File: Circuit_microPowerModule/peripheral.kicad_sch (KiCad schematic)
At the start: 26 parts, among them J4 Conn_01x05_Pin, J6 MikroBus

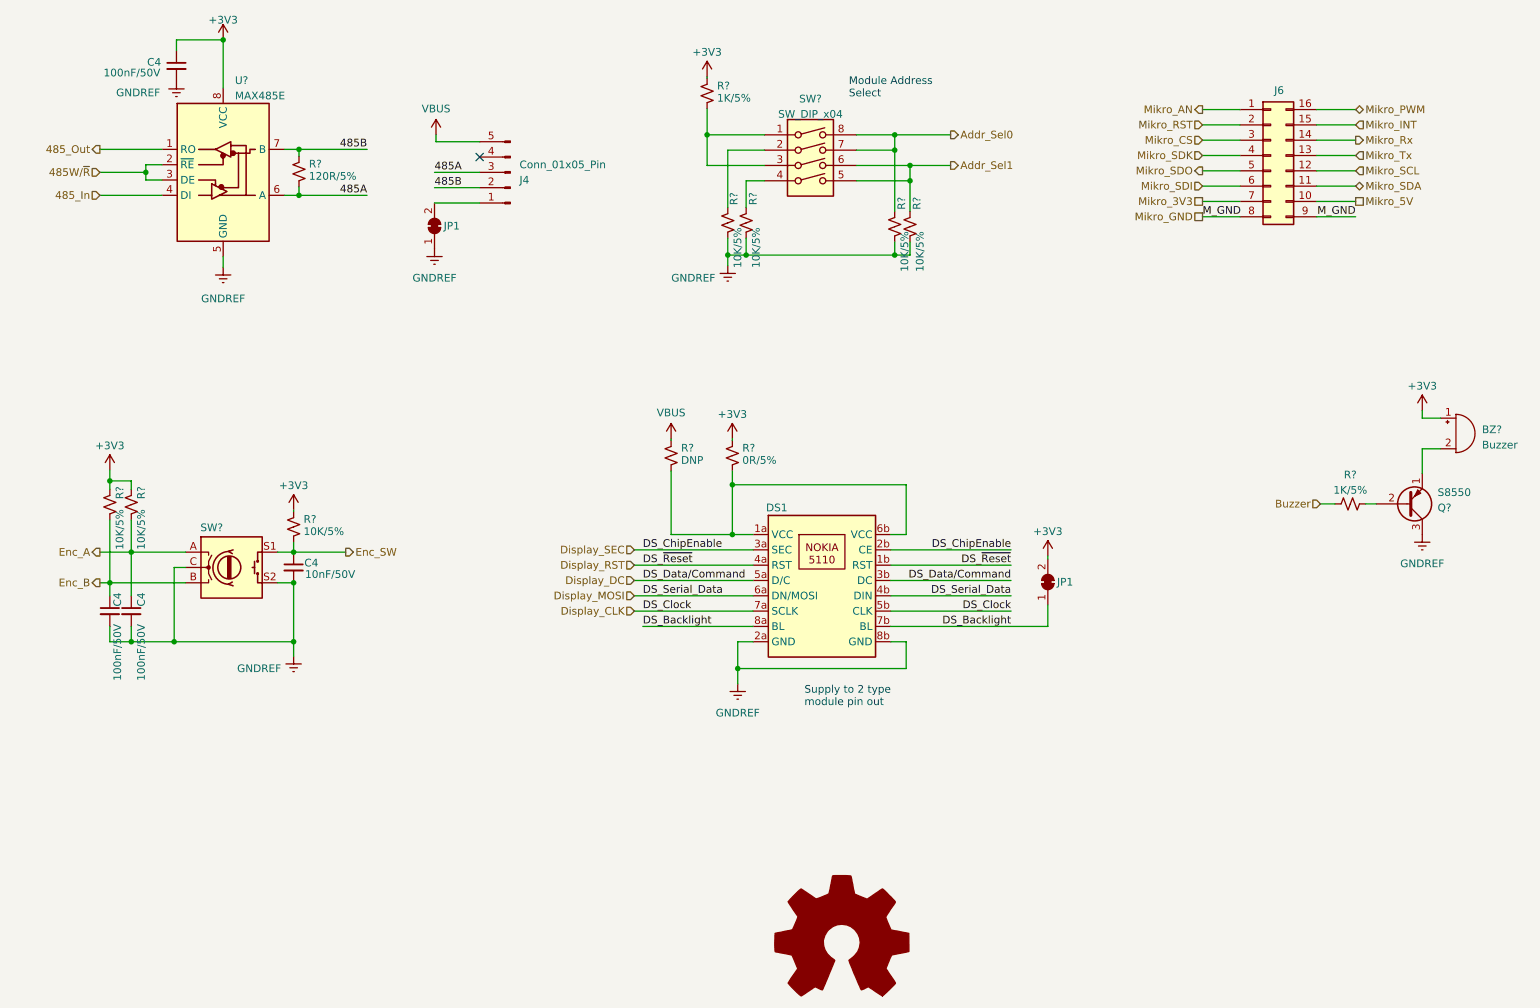
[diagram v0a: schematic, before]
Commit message: update schematic
added pin assessment to readme
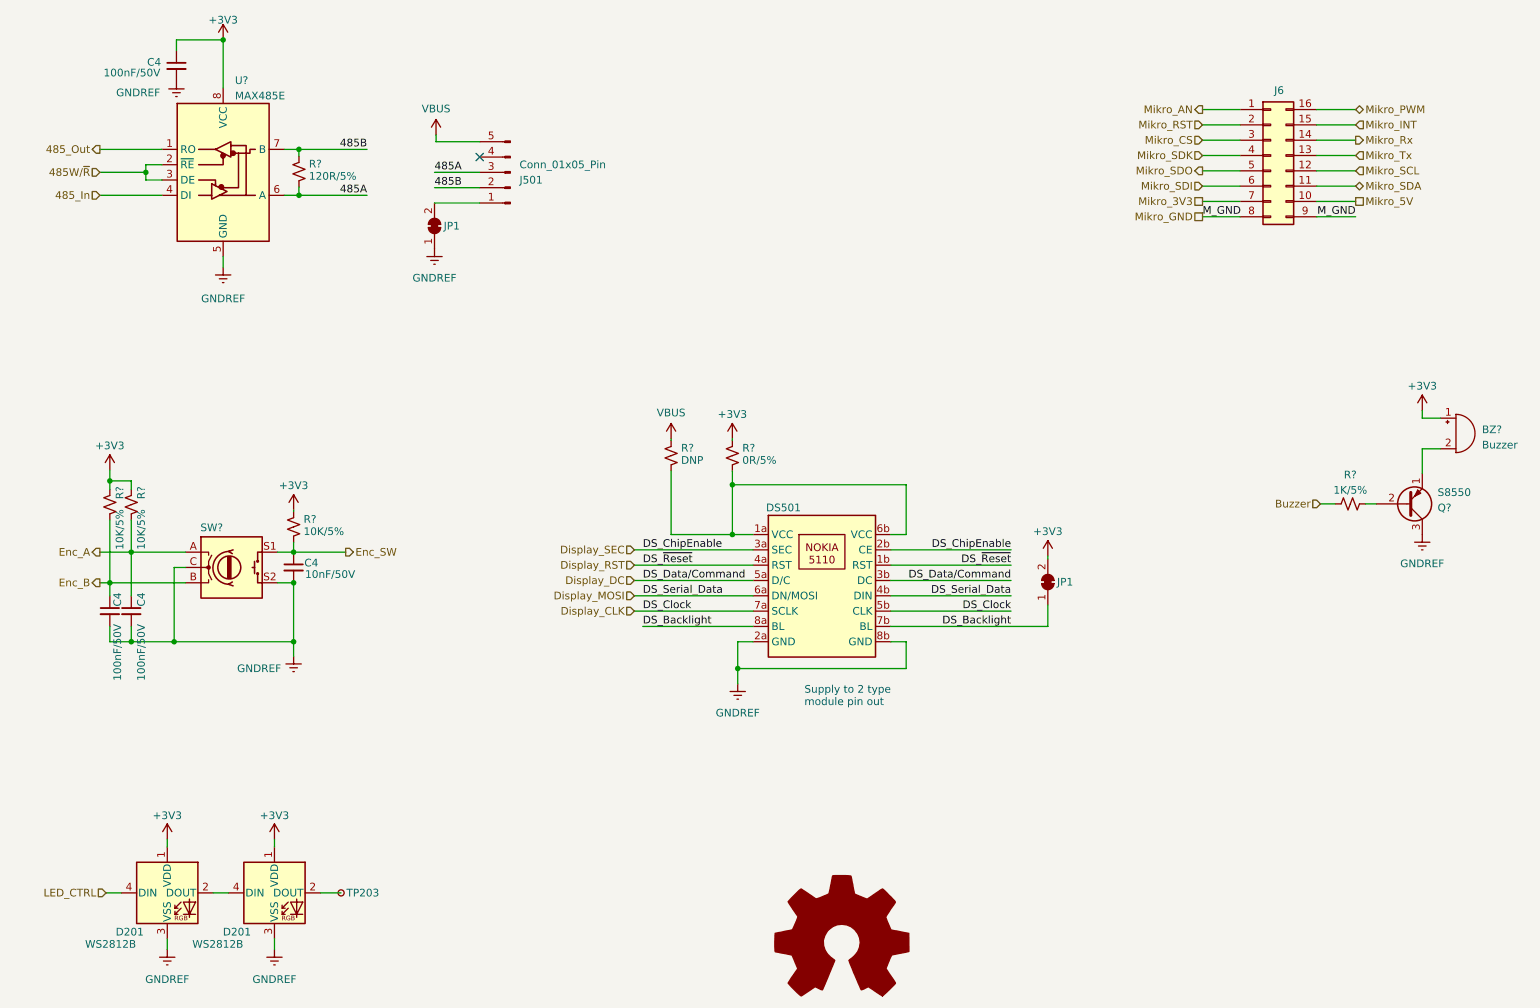
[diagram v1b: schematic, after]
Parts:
- removed R? (x4): 10K/5%, Resistor_SMD:R_0603_1608Metric, symbol Device:R_Small_US
- removed R?: 1K/5%, Resistor_SMD:R_0603_1608Metric, symbol Device:R_Small_US
- removed SW?: SW_DIP_x04, Button_Switch_SMD:SW_DIP_SPSTx04_Slide_Copal_CHS-04B_W7.62mm_P1.27mm, symbol Switch:SW_DIP_x04
- added D201 (x2): WS2812B, LED_SMD:LED_WS2812B_PLCC4_5.0x5.0mm_P3.2mm, symbol LED:WS2812B
- added TP203: TestPoint_Small, TestPoint:TestPoint_Keystone_5015_Micro-Minature, symbol Connector:TestPoint_Small
- renumbered DS1 to DS501, J4 to J501
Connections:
- net +3V3: now also D201.1 (VDD), D201.1 (VDD)
- net GNDREF: now also D201.3 (VSS), D201.3 (VSS)
- new net: D201.2 (DOUT), TP203.1
- new net: D201.2 (DOUT), D201.4 (DIN)
- new net LED_CTRL: D201.4 (DIN)

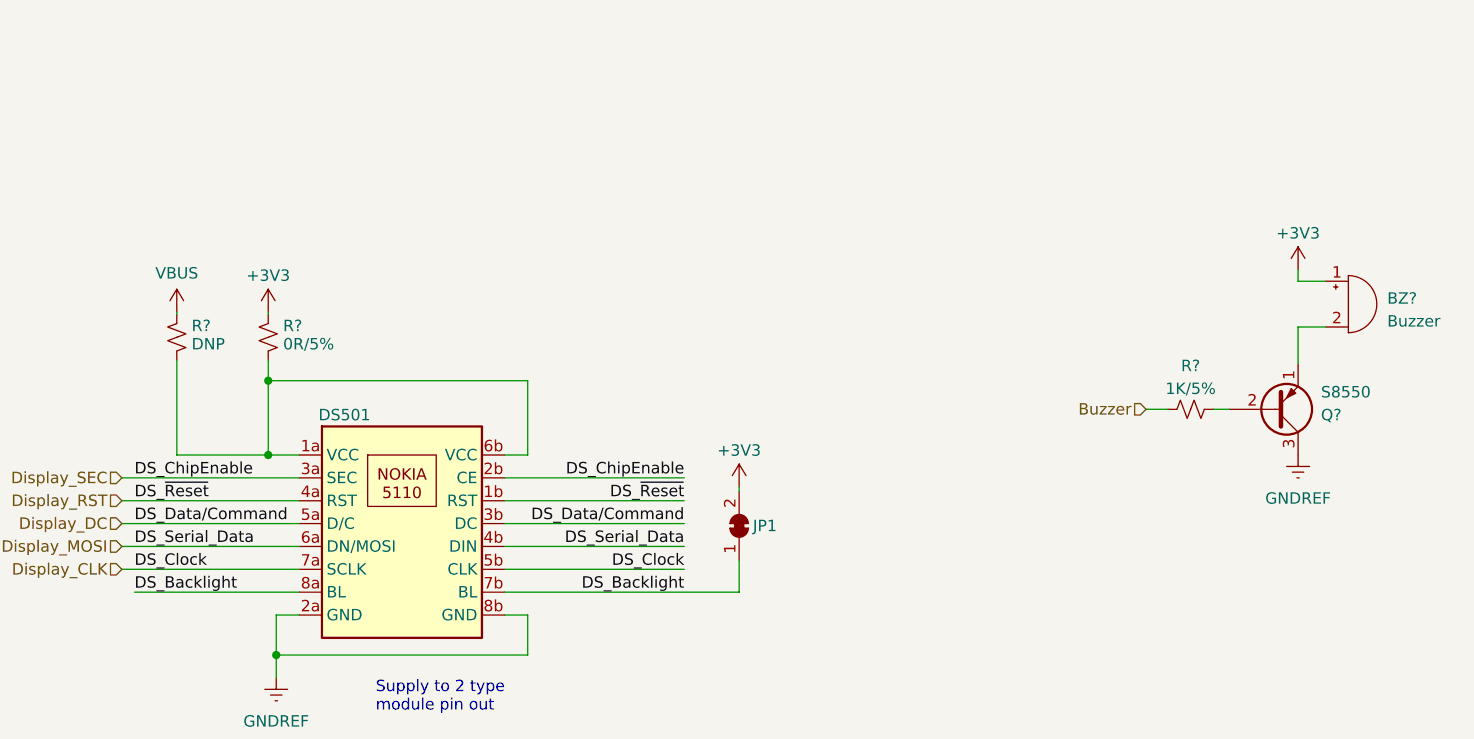
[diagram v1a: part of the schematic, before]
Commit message: modify ERC error, protect components
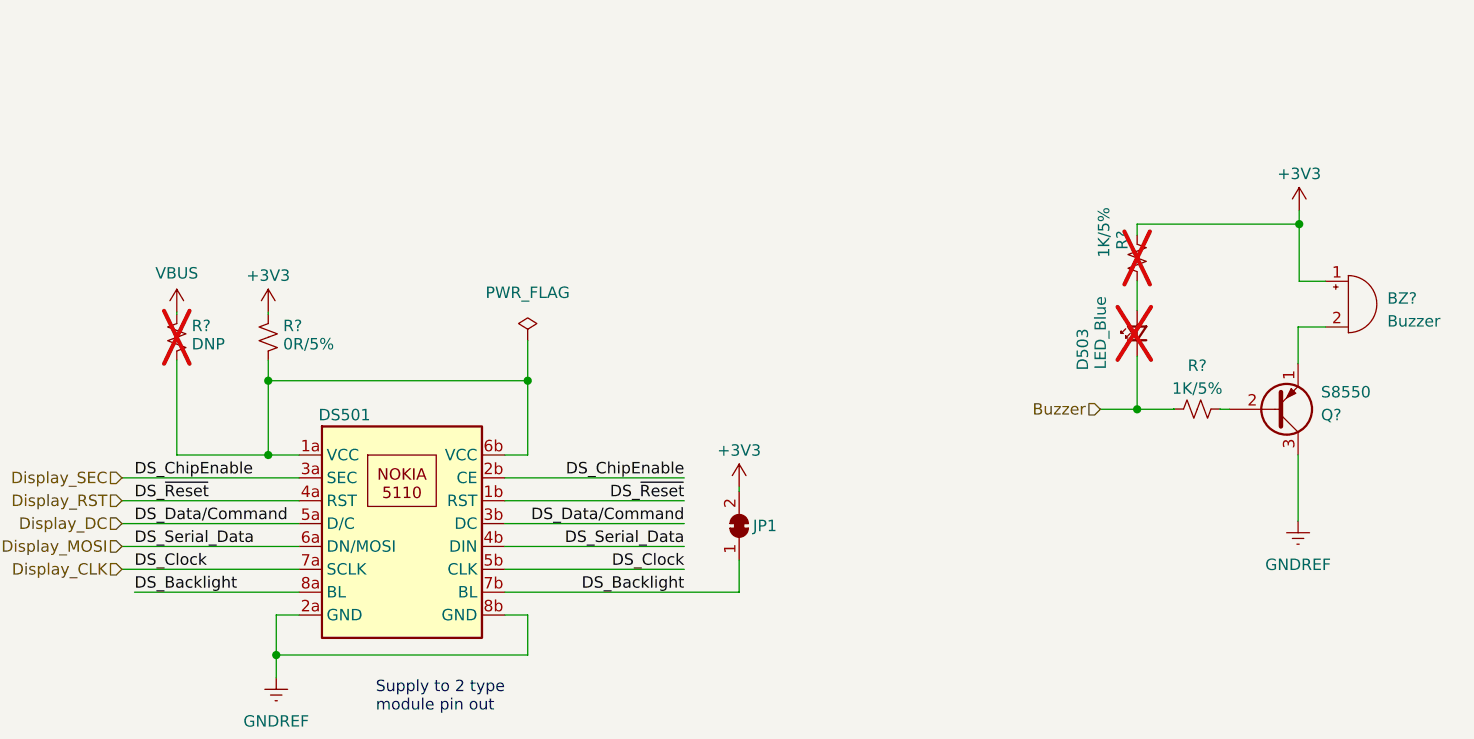
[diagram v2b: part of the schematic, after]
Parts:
- added D503: LED_Blue, LED_SMD:LED_1206_3216Metric, symbol Device:LED_Small
- added R?: 1K/5%, Resistor_SMD:R_0603_1608Metric, symbol Device:R_Small_US
- R?: now not fitted
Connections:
- net +3V3: now also R?.1
- net Buzzer: now also D503.1 (K)
- new net: D503.2 (A), R?.2
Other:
- title: (none) -> µPower Module
- moved on the sheet: R?

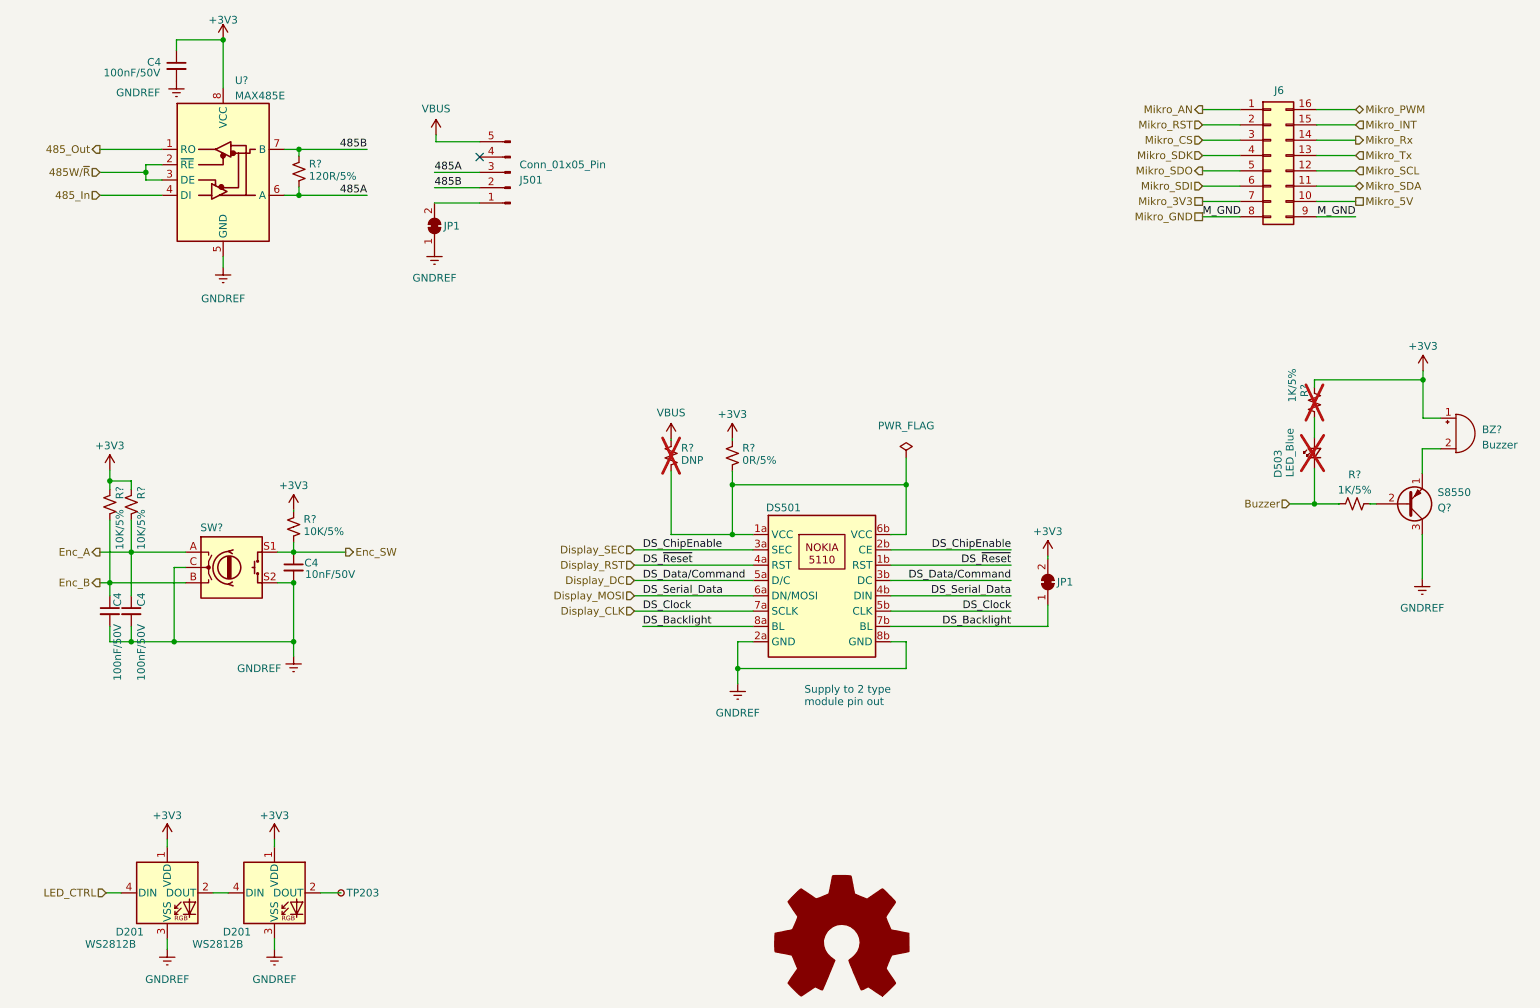
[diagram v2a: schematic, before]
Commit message: modify ERC warning
modify OPA, TVS-Diode, Cap
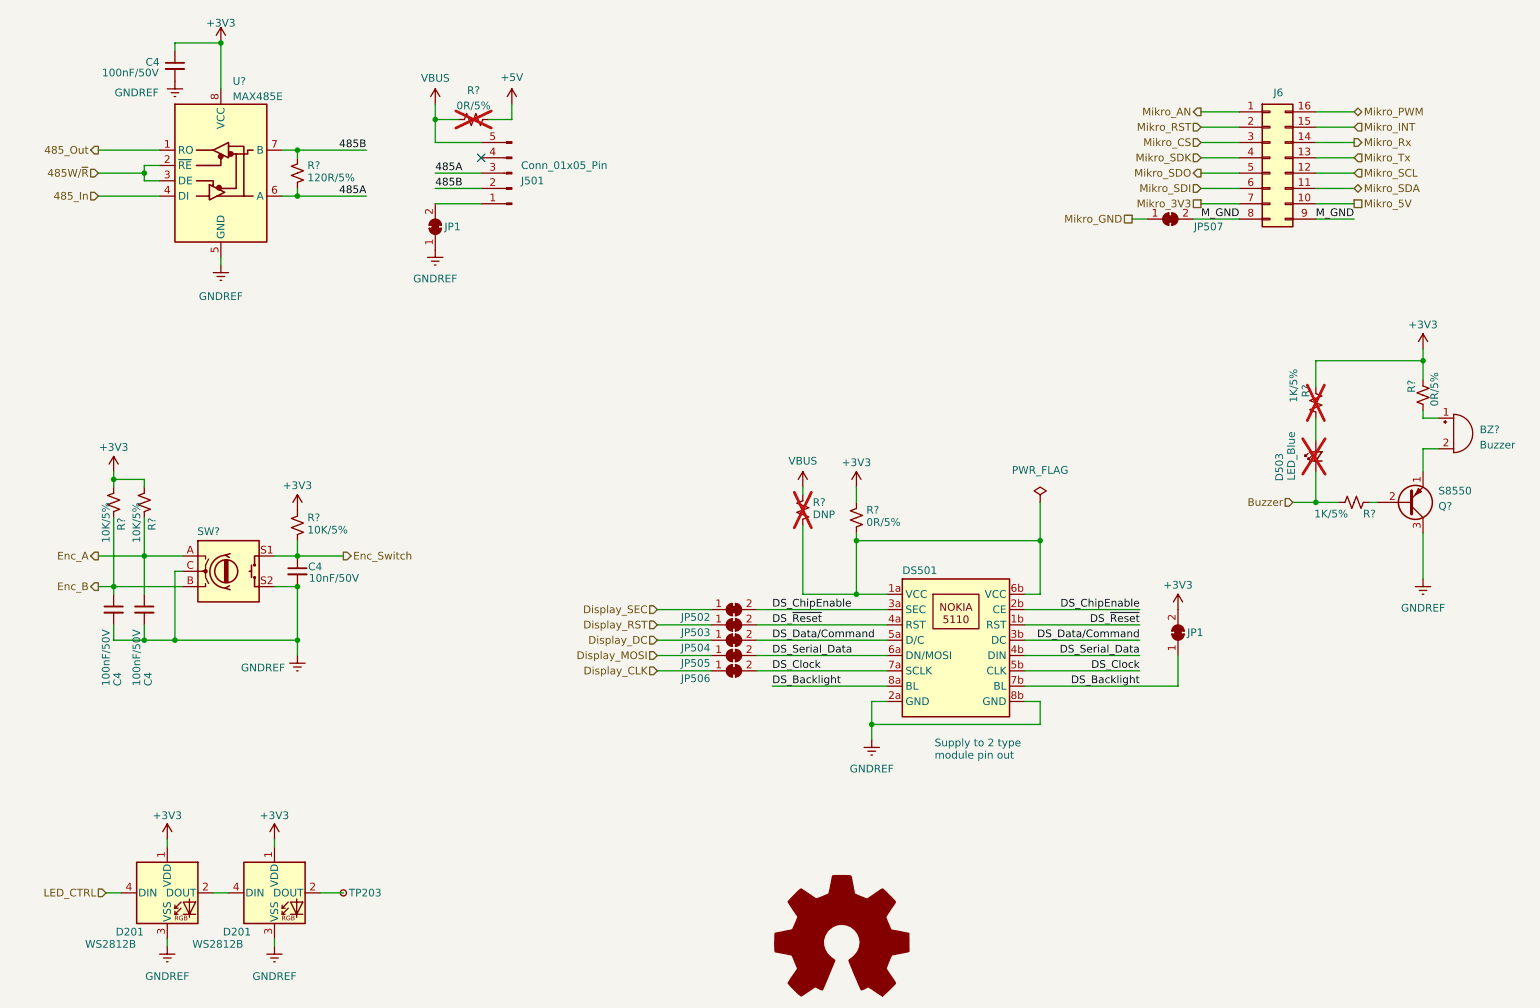
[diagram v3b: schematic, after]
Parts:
- added JP502, JP503, JP504, JP505, JP506, JP507: SolderJumper_2_Bridged, Jumper:SolderJumper-2_P1.3mm_Bridged_Pad1.0x1.5mm, symbol Jumper:SolderJumper_2_Bridged
- added R? (x2): 0R/5%, Resistor_SMD:R_0603_1608Metric, symbol Device:R_Small_US
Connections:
- net +3V3: now also R?.1; no longer BZ?.1 (-)
- net Display_CLK: now also JP506.1 (A); no longer DS501.5b (CLK), DS501.7a (SCLK)
- net Display_DC: now also JP504.1 (A); no longer DS501.3b (DC), DS501.5a (D/C)
- net Display_MOSI: now also JP505.1 (A); no longer DS501.4b (DIN), DS501.6a (DN/MOSI)
- net Display_RST: now also JP503.1 (A); no longer DS501.1b (RST), DS501.4a (RST)
- net Display_SEC: now also JP502.1 (A); no longer DS501.2b (CE), DS501.3a (SEC)
- net Mikro_GND: now also JP507.1 (A); no longer J6.8 (Pin_8), J6.9 (Pin_9)
- net VBUS: now also R?.1
- net Enc_SW renamed Enc_Switch
- new net: BZ?.1 (-), R?.2
- new net +5V: R?.2
- new net DS_ChipEnable: DS501.2b (CE), DS501.3a (SEC), JP502.2 (B)
- new net DS_Clock: DS501.5b (CLK), DS501.7a (SCLK), JP506.2 (B)
- new net DS_Data/Command: DS501.3b (DC), DS501.5a (D/C), JP504.2 (B)
- new net DS_Serial_Data: DS501.4b (DIN), DS501.6a (DN/MOSI), JP505.2 (B)
- new net DS_~{Reset}: DS501.1b (RST), DS501.4a (RST), JP503.2 (B)
- new net M_GND: J6.8 (Pin_8), J6.9 (Pin_9), JP507.2 (B)
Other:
- moved on the sheet: C4, D503, DS501, JP1, R?, SW?

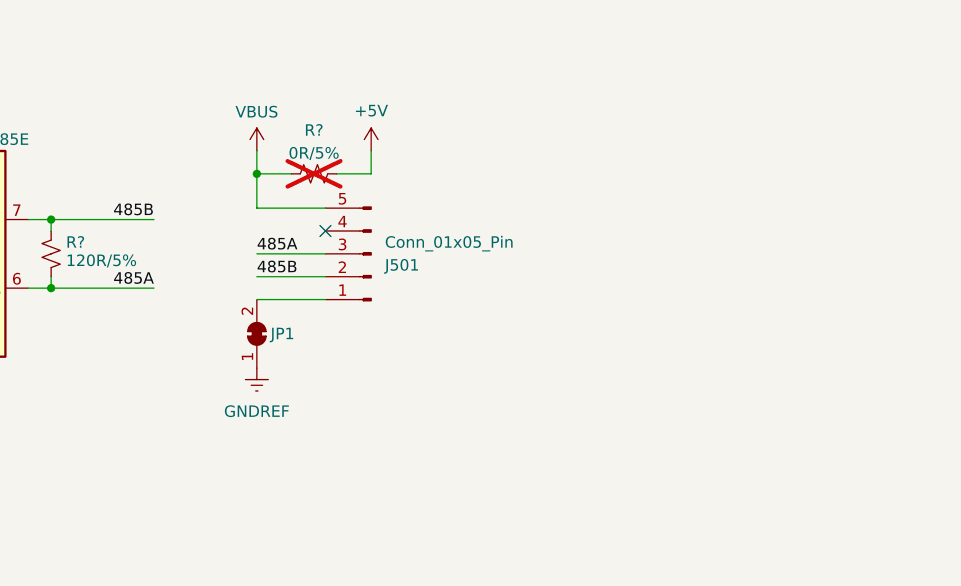
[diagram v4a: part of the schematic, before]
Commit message: update pcb layout component
target to smaller pcb size
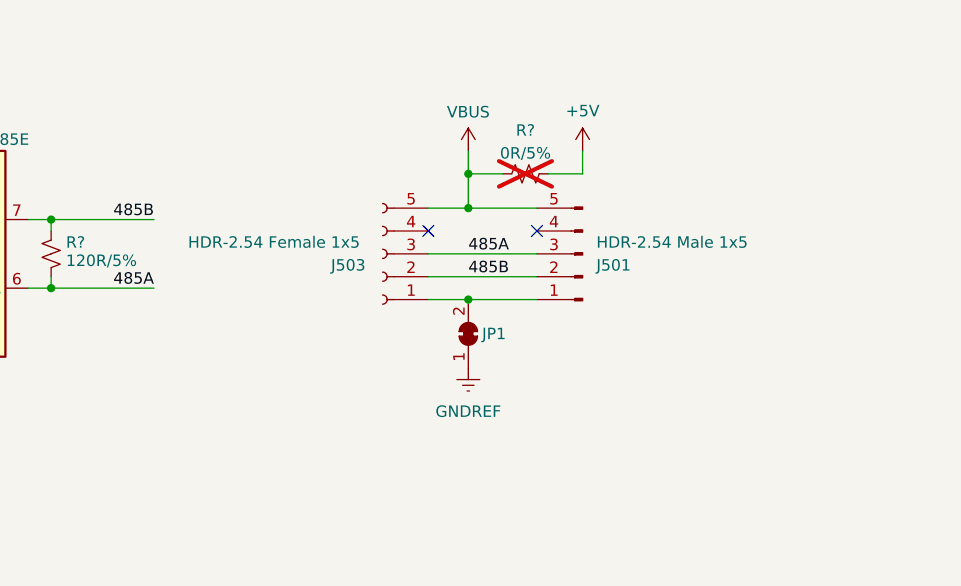
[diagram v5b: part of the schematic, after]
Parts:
- added J503: HDR-2.54 Female 1x5, Connector_PinSocket_2.54mm:PinSocket_1x05_P2.54mm_Vertical, symbol Connector:Conn_01x05_Socket
- J501: value Conn_01x05_Pin -> HDR-2.54 Male 1x5
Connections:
- net 485A: now also J503.3 (Pin_3)
- net 485B: now also J503.2 (Pin_2)
- net VBUS: now also J503.5 (Pin_5)
- net at J501.1 (Pin_1), JP1.2 (B): now also J503.1 (Pin_1)
- no-connect marks 1 -> 2
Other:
- moved on the sheet: J501, JP1, R?
